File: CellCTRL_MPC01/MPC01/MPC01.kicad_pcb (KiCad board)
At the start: 4 copper layers, 95.8 x 62 mm, 51 parts, among them J1 Power 24V, J10 Microstepping, J11 Microstepping, J12 StepMotor 1, J13 StepMotor 2, J14 StepMotor 3, J15 StepMotor 4, J16 Conn_01x05_Pin, J2 Conn_01x03_Pin, J3 Servo Motor 1u2, J4 Endstop X, J5 Endstop Y, J6 Endstop Z, J7 0Ohm Jumper, J8 Microstepping, J9 Microstepping, U1 TP8485E-SR

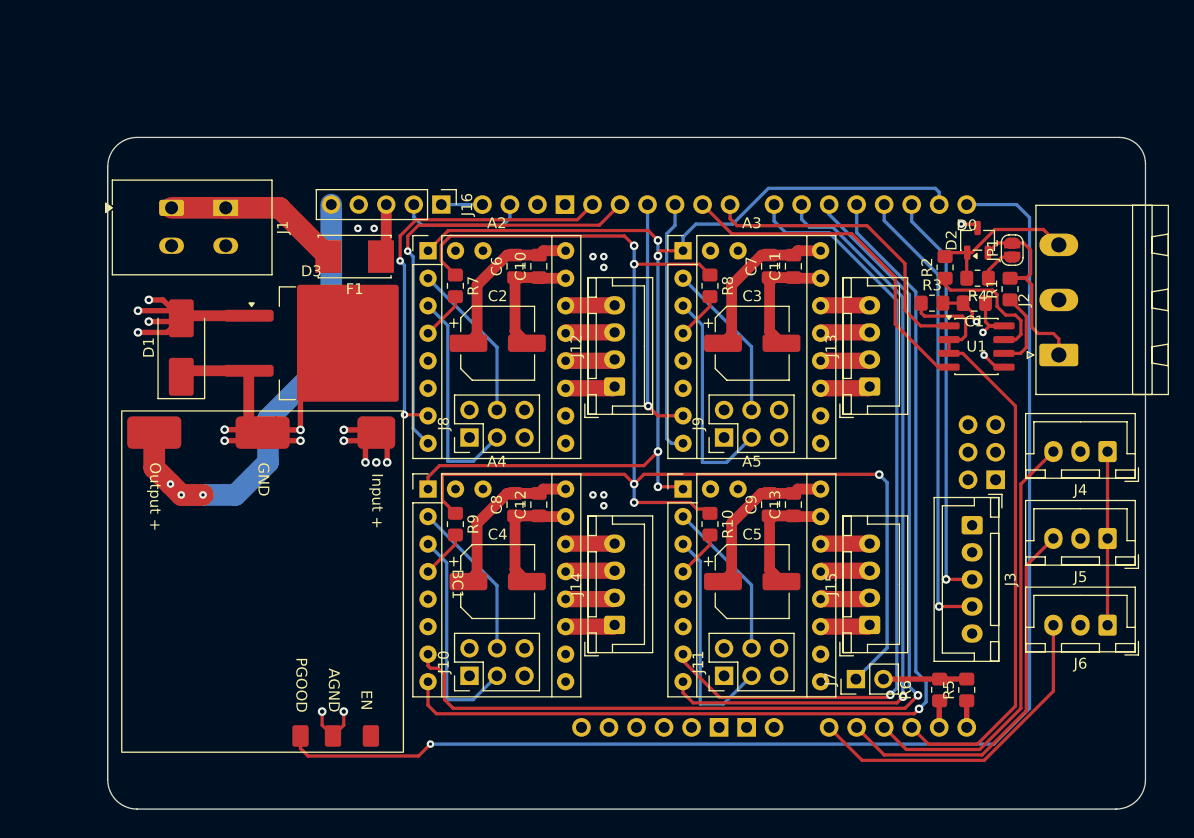
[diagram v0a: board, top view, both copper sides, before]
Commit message: Silkscreen Add Files
Hinzufügen der Beschriftungen auf dem Silkscreen FRont and Back
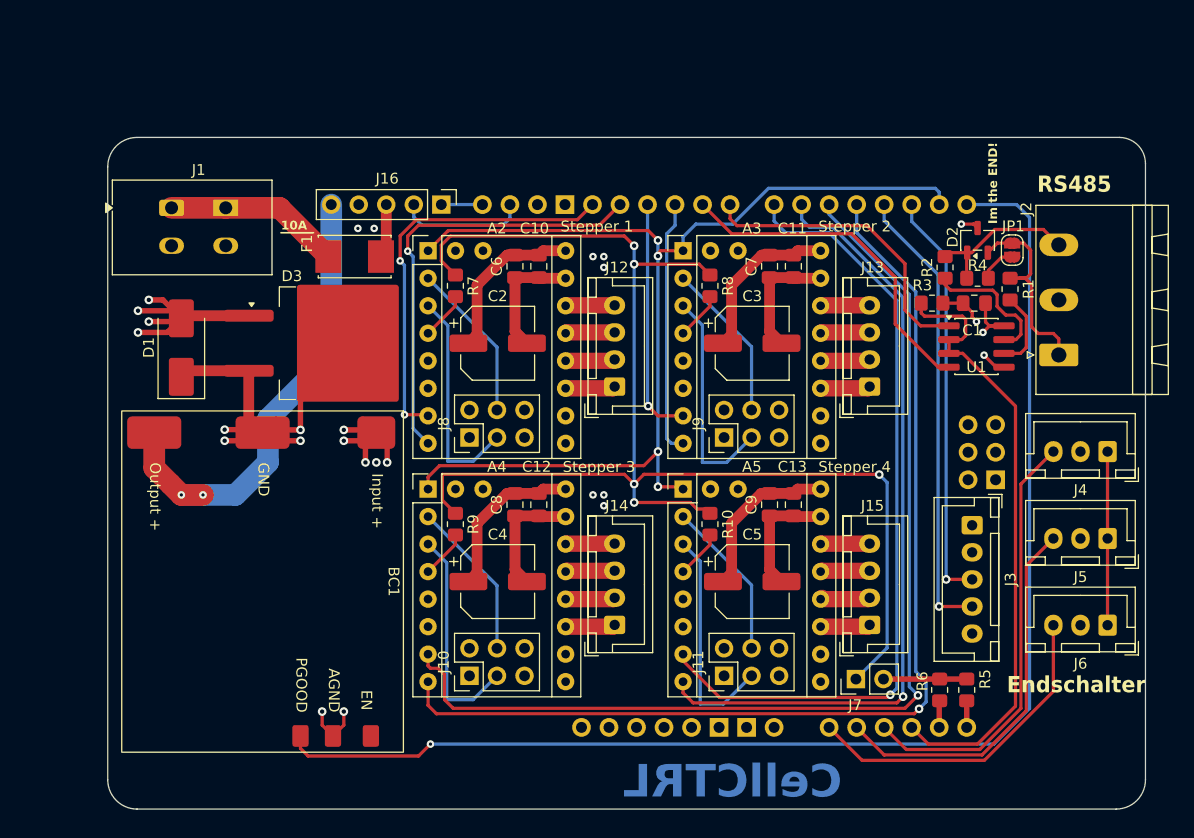
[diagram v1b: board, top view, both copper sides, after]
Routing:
- net 5V: vias 4 -> 3
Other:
- board text added: "10A"
- board text added: "2026/02 V0.1b Edited by: KJ"
- board text added: "CellCTRL"
- board text added: "Endschalter"
- board text added: "Im the END!"
- board text added: "MPC01"
- board text added: "RS485"
- board text added: "Stepper 1"
- board text added: "Stepper 2"
- board text added: "Stepper 3"
- board text added: "Stepper 4"
- board text added: "This Product is designed and made for KTLA/Litec"

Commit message: Update MPC01
MPC01 update
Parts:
- removed A5: TMC2209, MPC01_lib:TMC2209
- removed C11, C12, C13: 4,7uF, Capacitor_SMD:C_0805_2012Metric_Pad1.18x1.45mm_HandSolder
- removed J12: StepMotor 1, Connector_JST:JST_XH_B4B-XH-A_1x04_P2.50mm_Vertical
- removed J13: StepMotor 2, Connector_JST:JST_XH_B4B-XH-A_1x04_P2.50mm_Vertical
- removed J14: StepMotor 3, Connector_JST:JST_XH_B4B-XH-A_1x04_P2.50mm_Vertical
- removed J15: StepMotor 4, Connector_JST:JST_XH_B4B-XH-A_1x04_P2.50mm_Vertical
- removed J16: Conn_01x05_Pin, Connector_PinHeader_2.54mm:PinHeader_1x05_P2.54mm_Vertical
- added JP10: Jumper_2_Open, Jumper:SolderJumper-2_P1.3mm_Open_RoundedPad1.0x1.5mm, F.Cu at (137.1, 50.2)
- added JP2: MS1, Connector_PinHeader_2.54mm:PinHeader_1x02_P2.54mm_Vertical, F.Cu at (95.5, 71.7)
- added JP3: MS1, Connector_PinHeader_2.54mm:PinHeader_1x02_P2.54mm_Vertical, F.Cu at (121.5, 71.7)
- added JP4: MS2, Connector_PinHeader_2.54mm:PinHeader_1x02_P2.54mm_Vertical, F.Cu at (102.5, 45.4)
- added JP5: MS2, Connector_PinHeader_2.54mm:PinHeader_1x02_P2.54mm_Vertical, F.Cu at (95.5, 68.1)
- added JP6: MS2, Connector_PinHeader_2.54mm:PinHeader_1x02_P2.54mm_Vertical, F.Cu at (121.5, 68.1)
- added JP7: Jumper_3_Open, PCM_SparkFun-Jumper:Jumper_3_NO, F.Cu at (96.8, 51.6)
- added JP8: Jumper_3_Open, PCM_SparkFun-Jumper:Jumper_3_NO, F.Cu at (89.8, 74.3)
- added JP9: Jumper_3_Open, PCM_SparkFun-Jumper:Jumper_3_NO, F.Cu at (115.8, 74.3)
- added R11: 120R, Resistor_SMD:R_0805_2012Metric_Pad1.20x1.40mm_HandSolder, F.Cu at (136.6, 46.2)
- added R12: 10R, Resistor_SMD:R_0805_2012Metric_Pad1.20x1.40mm_HandSolder, F.Cu at (134.6, 46.2)
- added R13: 10K, Resistor_SMD:R_0805_2012Metric_Pad1.20x1.40mm_HandSolder, F.Cu at (129.6, 52.2)
- added R14: 10K, Resistor_SMD:R_0805_2012Metric_Pad1.20x1.40mm_HandSolder, F.Cu at (116.0, 59.2)
- added R15: 1K, Resistor_SMD:R_0805_2012Metric_Pad1.20x1.40mm_HandSolder, F.Cu at (118.0, 61.3)
- added R16: 1K, Resistor_SMD:R_0805_2012Metric_Pad1.20x1.40mm_HandSolder, F.Cu at (118.8, 43.5)
- added R17: 1K, Resistor_SMD:R_0805_2012Metric_Pad1.20x1.40mm_HandSolder, F.Cu at (118.8, 41.4)
- A1: value Arduino_Uno_R3_Shield -> TMC2209; footprint PCM_arduino-library:Arduino_Uno_R3_Shield -> MPC01_lib:TMC2209
- A4: value TMC2209 -> Arduino_Uno_R3_Shield; footprint MPC01_lib:TMC2209 -> PCM_arduino-library:Arduino_Uno_R3_Shield
- C1: value 100n -> 100uf; footprint Capacitor_SMD:C_0805_2012Metric_Pad1.18x1.45mm_HandSolder -> Capacitor_SMD:CP_Elec_6.3x7.7
- C10: value 4,7uF -> 100n
- C2, C5: value 100uf -> 1uF; footprint Capacitor_SMD:CP_Elec_6.3x7.7 -> Capacitor_SMD:C_0805_2012Metric_Pad1.18x1.45mm_HandSolder
- C3: value 100uf -> 4,7uF; footprint Capacitor_SMD:CP_Elec_6.3x7.7 -> Capacitor_SMD:C_0805_2012Metric_Pad1.18x1.45mm_HandSolder
- C6, C9: value 1uF -> 4,7uF
- C7: value 1uF -> 100uf; footprint Capacitor_SMD:C_0805_2012Metric_Pad1.18x1.45mm_HandSolder -> Capacitor_SMD:CP_Elec_6.3x7.7
- D1: value D_TVS -> SM712_SOT23; footprint Diode_SMD:D_SMB_Handsoldering -> Package_TO_SOT_SMD:SOT-23-3
- D2: value SM712_SOT23 -> D_TVS; footprint Package_TO_SOT_SMD:SOT-23-3 -> Diode_SMD:D_SMB_Handsoldering
- J1: value Power 24V -> StepMotor 1; footprint TerminalBlock_WAGO:TerminalBlock_WAGO_2601-1102_1x02_P3.50mm_Horizontal -> Connector_JST:JST_XH_B4B-XH-A_1x04_P2.50mm_Vertical
- J10: value Microstepping -> Enable/Disable; footprint MPC01_lib:PinHeader_2x03_P2.54mm_Vertical_ Pinorder -> Connector_JST:JST_XH_B2B-XH-A_1x02_P2.50mm_Vertical
- J11: value Microstepping -> Endstop Z; footprint MPC01_lib:PinHeader_2x03_P2.54mm_Vertical_ Pinorder -> Connector_JST:JST_XH_B3B-XH-A_1x03_P2.50mm_Vertical
- J2: value Conn_01x03_Pin -> StepMotor 2; footprint Connector_Phoenix_MSTB:PhoenixContact_MSTBA_2,5_3-G-5,08_1x03_P5.08mm_Horizontal -> Connector_JST:JST_XH_B4B-XH-A_1x04_P2.50mm_Vertical
- J3: value Servo Motor 1u2 -> StepMotor 3; footprint Connector_JST:JST_XH_B5B-XH-A_1x05_P2.50mm_Vertical -> Connector_JST:JST_XH_B4B-XH-A_1x04_P2.50mm_Vertical
- J4: value Endstop X -> Conn_01x03_Pin; footprint Connector_JST:JST_XH_B3B-XH-A_1x03_P2.50mm_Vertical -> Connector_Phoenix_MSTB:PhoenixContact_MSTBA_2,5_3-G-5,08_1x03_P5.08mm_Horizontal
- J5: value Endstop Y -> I2C; footprint Connector_JST:JST_XH_B3B-XH-A_1x03_P2.50mm_Vertical -> Connector_JST:JST_XH_B5B-XH-A_1x05_P2.50mm_Vertical
- J6: value Endstop Z -> Endstop X
- J7: value 0Ohm Jumper -> Power 24V; footprint Connector_PinHeader_2.54mm:PinHeader_1x02_P2.54mm_Vertical -> TerminalBlock_WAGO:TerminalBlock_WAGO_2601-1102_1x02_P3.50mm_Horizontal
- J8: value Microstepping -> 0Ohm Jumper; footprint MPC01_lib:PinHeader_2x03_P2.54mm_Vertical_ Pinorder -> Connector_PinHeader_2.54mm:PinHeader_1x02_P2.54mm_Vertical
- J9: value Microstepping -> Endstop Y; footprint MPC01_lib:PinHeader_2x03_P2.54mm_Vertical_ Pinorder -> Connector_JST:JST_XH_B3B-XH-A_1x03_P2.50mm_Vertical
- JP1: value Jumper_2_Open -> MS1; footprint Jumper:SolderJumper-2_P1.3mm_Open_RoundedPad1.0x1.5mm -> Connector_PinHeader_2.54mm:PinHeader_1x02_P2.54mm_Vertical
- R1, R2: value 10R -> 10K
- R10: value 1K -> 10R
- R4: value 120R -> 10K
- R5, R6: value 1K -> 10K
- moved J7 81.6 mm to (68.0, 44.0), turned to 180 degrees
- moved D1 69.6 mm to (137.5, 41.9)
- moved D2 69.5 mm to (76.0, 40.5), turned to 0 degrees
- moved A1 61.5 mm to (97.8, 41.1)
- moved R1 58.5 mm to (89.8, 66.8), turned to -90 degrees
- moved R4 56.6 mm to (89.8, 70.8), turned to 90 degrees
- moved J1 47.0 mm to (116.8, 55.1), turned to 90 degrees
- moved R3 45.8 mm to (96.8, 44.1), turned to -90 degrees
- moved JP1 45.5 mm to (102.5, 49.0)
- moved R2 45.3 mm to (96.8, 48.1)
- moved J2 44.5 mm to (110.0, 77.8)
- moved J10 43.6 mm to (124.0, 58.0), turned to 0 degrees
- moved J11 38.9 mm to (143.0, 60.5), turned to 0 degrees
- moved C1 37.5 mm to (106.8, 56.6), turned to -90 degrees
- moved R6 37.1 mm to (115.8, 66.8), turned to -90 degrees
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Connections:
- A2 pad 5: unconnected-(A2-TX-Pad5) -> Net-(A2-TX)
- A2 pad 7: STEP1 -> STEP2
- A2 pad 8: DIR1 -> DIR2
- A3 pad 5: unconnected-(A3-TX-Pad5) -> Net-(A3-TX)
- A3 pad 7: STEP2 -> STEP3
- A3 pad 8: DIR2 -> DIR3
- C1 pad 1: 5V -> +24V
- C10 pad 1: GND -> 5V
- C10 pad 2: +24V -> GND
- C2 pad 1: +24V -> GND
- C2 pad 2: GND -> +24V
- C3 pad 1: +24V -> GND
- C3 pad 2: GND -> +24V
- C5 pad 1: +24V -> GND
- C5 pad 2: GND -> +24V
- C7 pad 1: GND -> +24V
- C7 pad 2: +24V -> GND
- D1 pad 1: GND -> Net-(D1-A1)
- D1 pad 2: +24V -> Net-(D1-A2)
- D2 pad 1: Net-(D2-A1) -> GND
- D2 pad 2: Net-(D2-A2) -> +24V
- F1 pad 2: Net-(J1-Pin_1) -> Net-(J7-Pin_1)
- J1 pad 1: Net-(J1-Pin_1) -> Net-(A1-B2)
- J1 pad 2: GND -> Net-(A1-B1)
- J10 pad 1: 5V -> ENABLE
- J10 pad 2: Net-(A4-MS2) -> GND
- J11 pad 1: 5V -> Net-(J11-Pin_1)
- J11 pad 2: Net-(A5-MS2) -> GND
- J11 pad 3: GND -> EndstopZ
- J2 pad 1: Net-(D2-A2) -> Net-(A2-B2)
- J2 pad 2: GND -> Net-(A2-B1)
- J2 pad 3: Net-(D2-A1) -> Net-(A2-A1)
- J3 pad 1: GND -> Net-(A3-B2)
- J3 pad 2: 5V -> Net-(A3-B1)
- J3 pad 3: Motor1 -> Net-(A3-A1)
- J3 pad 4: Motor2 -> Net-(A3-A2)
- J4 pad 1: Net-(J4-Pin_1) -> Net-(D1-A2)
- J4 pad 3: EndstopX -> Net-(D1-A1)
- J5 pad 1: Net-(J4-Pin_1) -> Net-(J5-Pin_1)
- J5 pad 2: GND -> Net-(J5-Pin_2)
- J5 pad 3: EndstopY -> +24V
- J6 pad 1: Net-(J4-Pin_1) -> Net-(J11-Pin_1)
- J6 pad 3: EndstopZ -> EndstopX
- J7 pad 1: PDNUart -> Net-(J7-Pin_1)
- J7 pad 2: Net-(J7-Pin_2) -> GND
- J8 pad 1: 5V -> PDNUart
- J8 pad 2: Net-(A2-MS2) -> Net-(J8-Pin_2)
- J9 pad 1: 5V -> Net-(J11-Pin_1)
- J9 pad 2: Net-(A3-MS2) -> GND
- J9 pad 3: GND -> EndstopY
- JP1 pad 1: Net-(JP1-A) -> Net-(A1-MS2)
- JP1 pad 2: Net-(D2-A2) -> 5V
- R1 pad 1: RS485_A -> GND
- R1 pad 2: Net-(D2-A2) -> Net-(A2-MS1)
- R10 pad 1: PDNUart -> RS485_A
- R10 pad 2: Net-(A5-RX) -> Net-(D1-A2)
- R2 pad 1: RS485_B -> GND
- R2 pad 2: Net-(D2-A1) -> Net-(A1-MS2)
- R3 pad 1: RS485_DE/RE -> GND
- R3 pad 2: GND -> Net-(A1-MS1)
- R4 pad 1: Net-(JP1-A) -> GND
- R4 pad 2: Net-(D2-A1) -> Net-(A2-MS2)
- R5 pad 1: RX -> GND
- R5 pad 2: Net-(J7-Pin_2) -> Net-(A3-MS2)
- R6 pad 1: TX -> GND
- R6 pad 2: Net-(J7-Pin_2) -> Net-(A3-MS1)
- R7 pad 1: PDNUart -> Net-(JP7-C)
- R7 pad 2: Net-(A2-RX) -> PDNUart
- R8 pad 1: PDNUart -> Net-(JP8-C)
- R8 pad 2: Net-(A3-RX) -> PDNUart
- R9 pad 1: PDNUart -> Net-(JP9-C)
- R9 pad 2: Net-(A4-RX) -> PDNUart
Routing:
- net STEP4: track 73.8 -> 0.00 mm, vias 1 -> 0
- net DIR4: track 72.5 -> 0.00 mm, vias 1 -> 0
- net PGOOD: track 122.2 -> 66.9 mm, vias 1 -> 2
- net STEP2: track 22.2 -> 72.4 mm, vias 1 -> 3
- net DIR2: track 23.6 -> 73.5 mm, vias 0 -> 3
- net Motor2: track 42.3 -> 0.00 mm, vias 1 -> 0
- net STEP3: track 98.5 -> 56.9 mm
- net DIR3: track 97.5 -> 56.4 mm
- net ENABLEOut: track 0.00 -> 39.3 mm, vias 0 -> 3
- net GND: track 99.2 -> 137.6 mm, vias 9 -> 12
- net Motor1: track 38.3 -> 0.00 mm, vias 1 -> 0
- net ENABLE: track 101.6 -> 66.4 mm, vias 4 -> 2
- net 5V: track 50.0 -> 15.8 mm
- net Net-(A5-MS2): track 21.2 -> 0.00 mm
- net Net-(A4-MS2): track 20.6 -> 0.00 mm
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- removed copper zone on In2.Cu, net +24V
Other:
- board size 95.8 x 62 mm -> 90.3 x 53.4 mm
- board text added: "(I2C)"
- board text added: "24V"
- board text added: "5V"
- board text added: "GND"
- board text added: "Motor 1 (X)"
- board text added: "Motor 2 (Y)"
- board text added: "Motor 3 (Z)"
- board text added: "Power In (24V DC)"
- board text added: "SCL"
- board text added: "SDA"
- board text added: "X-Endstop"
- board text added: "Y-Endstop"
- board text added: "Z-Endstop"
- board text removed: "10A"
- board text removed: "2026/02 V0.1b Edited by: KJ"
- board text removed: "CellCTRL"
- board text removed: "Endschalter"
- board text removed: "Im the END!"
- board text removed: "MPC01"
- board text removed: "Stepper 1"
- board text removed: "Stepper 2"
- board text removed: "Stepper 3"
- board text removed: "Stepper 4"
- board text removed: "This Product is designed and made for KTLA/Litec"

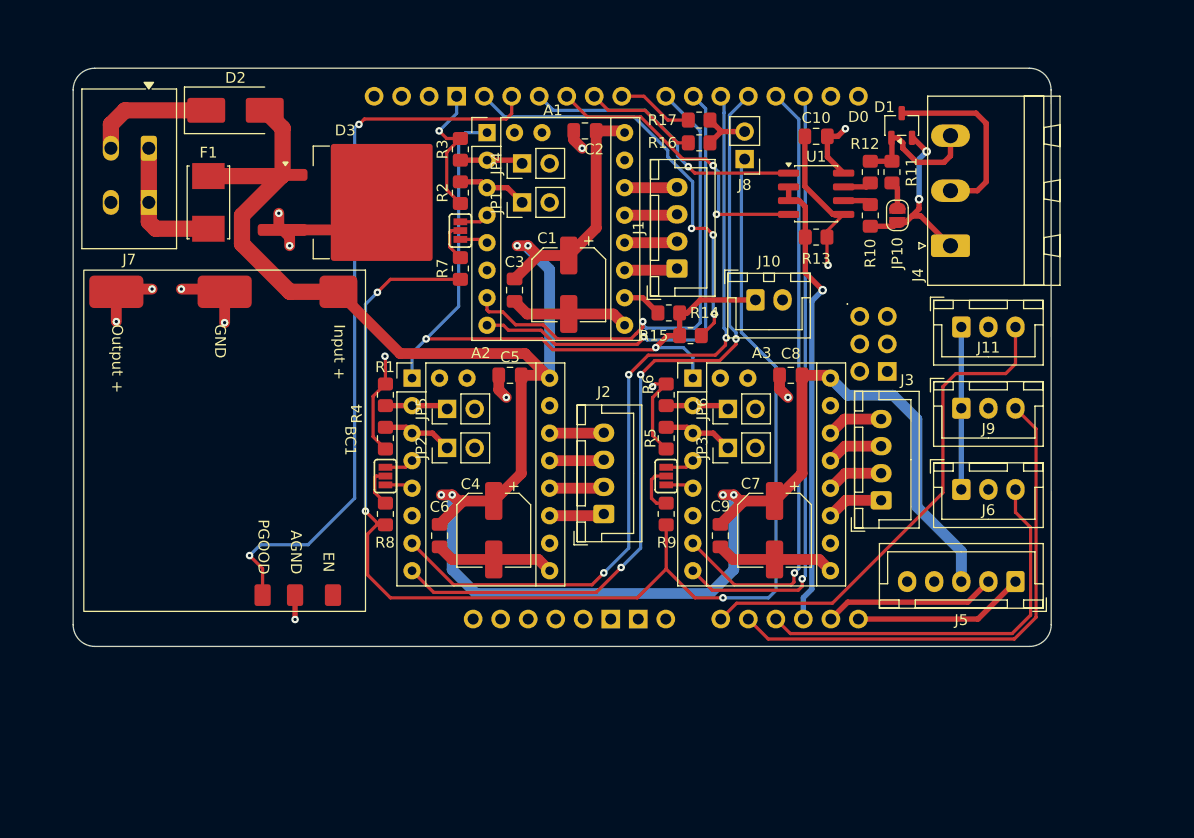
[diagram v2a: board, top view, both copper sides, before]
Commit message: Mounting Hole adds
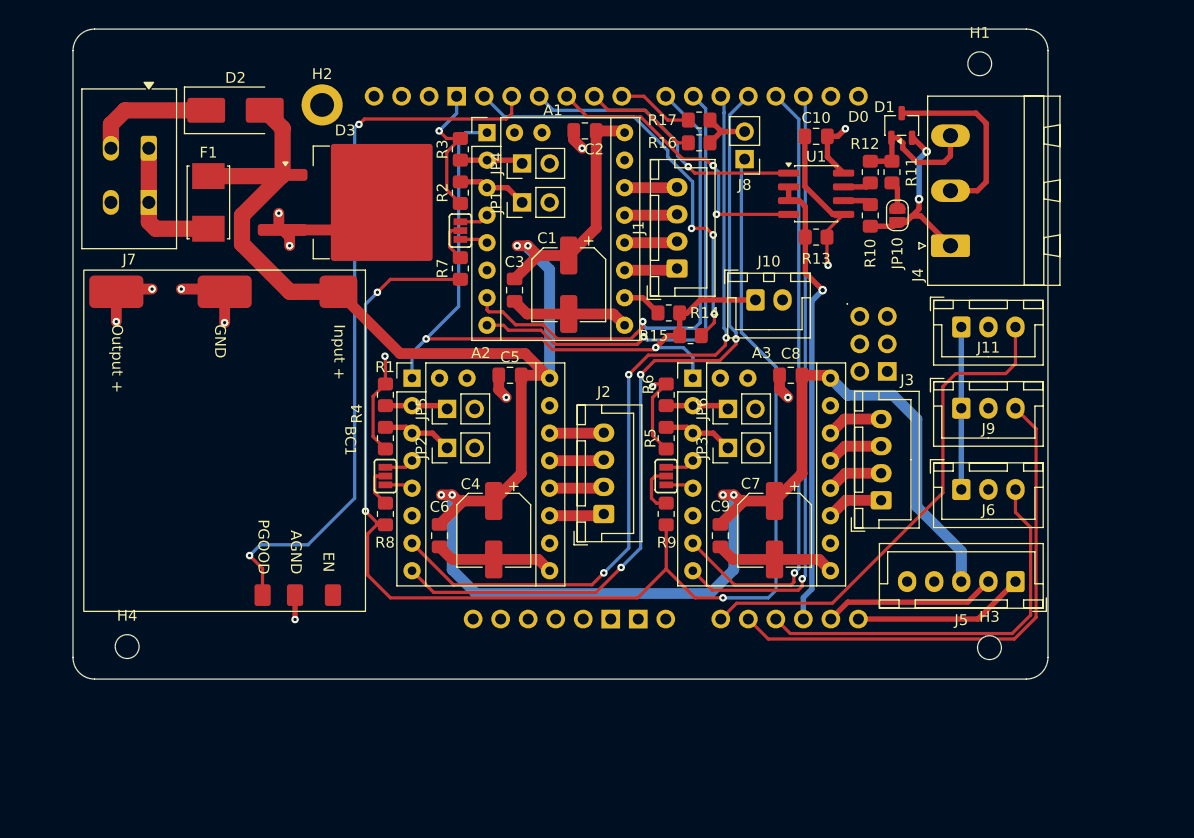
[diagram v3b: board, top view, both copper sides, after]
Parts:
- added H1: MountingHole, MountingHole:MountingHole_2.2mm_M2_DIN965, F.Cu at (144.7, 36.2)
- added H2: MountingHole_Pad, MountingHole:MountingHole_2.2mm_M2_DIN965_Pad, F.Cu at (84.0, 40.0)
- added H3: MountingHole, MountingHole:MountingHole_2.2mm_M2_DIN965, F.Cu at (145.6, 90.1)
- added H4: MountingHole, MountingHole:MountingHole_2.2mm_M2_DIN965, F.Cu at (66.0, 90.0)
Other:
- board size 90.3 x 53.4 mm -> 90 x 60 mm

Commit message: Maße
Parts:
- moved H2 18.6 mm to (66.0, 35.5)
- moved H1 1.48 mm to (146.0, 35.5)
- moved H3 0.72 mm to (146.0, 89.5)
- moved H4 0.50 mm to (66.0, 89.5)
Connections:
- A4 pad A4: Net-(J5-Pin_2) -> Net-(J5-Pin_1)
- A4 pad A5: Net-(J5-Pin_1) -> Net-(J5-Pin_2)
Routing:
- net Net-(J5-Pin_1): track 15.9 -> 20.2 mm
- net Net-(J5-Pin_2): track 16.0 -> 13.4 mm
- net EndstopX: track 37.0 -> 36.3 mm
- net EndstopY: track 48.2 -> 47.7 mm
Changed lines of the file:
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@@
 			(layers "*.Cu" "*.Mask")
 			(remove_unused_layers no)
-			(net 66 "Net-(J5-Pin_2)")
+			(net 58 "Net-(J5-Pin_1)")
 			(pinfunction "A4")
 			(pintype "bidirectional")
@@
 			(layers "*.Cu" "*.Mask")
 			(remove_unused_layers no)
-			(net 58 "Net-(J5-Pin_1)")
+			(net 66 "Net-(J5-Pin_2)")
 			(pinfunction "A5")
 			(pintype "bidirectional")
@@
 	(footprint "MountingHole:MountingHole_2.2mm_M2_DIN965_Pad"
 		(layer "F.Cu")
-		(at 84 40)
+		(at 66 35.5)
 		(descr "Mounting Hole 2.2mm, M2, generated by kicad-footprint-generator mountinghole.py")
 		(tags "mountinghole M2 DIN965")
 		(property "Reference" "H2"
-			(at 0 -2.85 0)
+			(at -3.5 0 0)
 			(layer "F.SilkS")
 			(effects
@@
 	(footprint "MountingHole:MountingHole_2.2mm_M2_DIN965"
 		(layer "F.Cu")
-		(at 145.6 90.1)
+		(at 146 89.5)
 		(descr "Mounting Hole 2.2mm, M2, no annular, generated by kicad-footprint-generator mountinghole.py")
 		(tags "mountinghole M2 DIN965")
 		(property "Reference" "H3"
-			(at 0 -2.85 0)
+			(at -4 0 0)
 			(layer "F.SilkS")
 			(effects
@@
 	(footprint "MountingHole:MountingHole_2.2mm_M2_DIN965"
 		(layer "F.Cu")
-		(at 66 90)
+		(at 66 89.5)
 		(descr "Mounting Hole 2.2mm, M2, no annular, generated by kicad-footprint-generator mountinghole.py")
 		(tags "mountinghole M2 DIN965")
 		(property "Reference" "H4"
-			(at 0 -2.85 0)
+			(at -3.5 0 0)
 			(layer "F.SilkS")
 			(effects
@@
 	(footprint "MountingHole:MountingHole_2.2mm_M2_DIN965"
 		(layer "F.Cu")
-		(at 144.7 36.2)
+		(at 146 35.5)
 		(descr "Mounting Hole 2.2mm, M2, no annular, generated by kicad-footprint-generator mountinghole.py")
 		(tags "mountinghole M2 DIN965")
 		(property "Reference" "H1"
-			(at 0 -2.85 0)
+			(at -4 0 0)
 			(layer "F.SilkS")
 			(effects
@@
 	)
 	(segment
-		(start 149.9 87.3)
-		(end 149.9 69.9)
+		(start 125.38 89.5)
+		(end 127.21148 89.5)
+		(width 0.3)
+		(layer "F.Cu")
+		(net 1)
+	)
+	(segment
+		(start 127.21148 89.5)
+		(end 127.41248 89.701)
 		(width 0.3)
 		(layer "F.Cu")
@@
 	)
 	(segment
-		(start 147.9 89.3)
-		(end 149.9 87.3)
+		(start 145.408521 86.8)
+		(end 148.9 86.8)
+		(width 0.3)
+		(layer "F.Cu")
+		(net 1)
+	)
+	(segment
+		(start 149.9 69.9)
+		(end 148 68)
 		(width 0.3)
 		(layer "F.Cu")
@@
 	(segment
 		(start 123.34 87.46)
-		(end 125.18 89.3)
+		(end 125.38 89.5)
 		(width 0.3)
 		(layer "F.Cu")
@@
 	)
 	(segment
-		(start 125.18 89.3)
-		(end 147.9 89.3)
+		(start 142.507521 89.701)
+		(end 145.408521 86.8)
 		(width 0.3)
 		(layer "F.Cu")
@@
 	)
 	(segment
-		(start 149.9 69.9)
-		(end 148 68)
+		(start 149.9 85.8)
+		(end 149.9 69.9)
+		(width 0.3)
+		(layer "F.Cu")
+		(net 1)
+	)
+	(segment
+		(start 127.41248 89.701)
+		(end 142.507521 89.701)
+		(width 0.3)
+		(layer "F.Cu")
+		(net 1)
+	)
+	(segment
+		(start 148.9 86.8)
+		(end 149.9 85.8)
 		(width 0.3)
 		(layer "F.Cu")
@@
 	)
 	(segment
-		(start 147.69248 88.799)
-		(end 149.399 87.09248)
+		(start 148 77.601)
+		(end 149.399 79)
 		(width 0.3)
 		(layer "F.Cu")
@@
 	)
 	(segment
-		(start 148 77.601)
-		(end 148 75.5)
+		(start 149.399 85.401)
+		(end 148.5 86.3)
 		(width 0.3)
 		(layer "F.Cu")
@@
 	)
 	(segment
-		(start 127.219 88.799)
-		(end 147.69248 88.799)
+		(start 142.3 89.2)
+		(end 127.62 89.2)
 		(width 0.3)
 		(layer "F.Cu")
@@
 	)
 	(segment
-		(start 125.88 87.46)
-		(end 127.219 88.799)
+		(start 149.399 79)
+		(end 149.399 85.401)
 		(width 0.3)
 		(layer "F.Cu")
@@
 	)
 	(segment
-		(start 149.399 87.09248)
-		(end 149.399 79)
+		(start 145.2 86.3)
+		(end 142.3 89.2)
 		(width 0.3)
 		(layer "F.Cu")
@@
 	)
 	(segment
-		(start 149.399 79)
+		(start 148 75.5)
 		(end 148 77.601)
 		(width 0.3)
@@
 	)
 	(segment
+		(start 148.5 86.3)
+		(end 145.2 86.3)
+		(width 0.3)
+		(layer "F.Cu")
+		(net 24)
+	)
+	(segment
+		(start 127.62 89.2)
+		(end 125.88 87.46)
+		(width 0.3)
+		(layer "F.Cu")
+		(net 24)
+	)
+	(segment
 		(start 89.84 75.0728)
 		(end 91.9928 75.0728)
@@
 	)
 	(segment
-		(start 148 84)
-		(end 144.54 87.46)
-		(width 0.5)
+		(start 130.96 87.46)
+		(end 132.1746 88.6746)
+		(width 0.3)
 		(layer "F.Cu")
 		(net 58)
 	)
 	(segment
-		(start 144.54 87.46)
-		(end 133.5 87.46)
-		(width 0.5)
+		(start 132.1746 88.6746)
+		(end 142.0254 88.6746)
+		(width 0.3)
 		(layer "F.Cu")
 		(net 58)
 	)
 	(segment
-		(start 143.6 85.9)
-		(end 145.5 84)
-		(width 0.5)
+		(start 144.9 85.8)
+		(end 147.4 85.8)
+		(width 0.3)
 		(layer "F.Cu")
-		(net 66)
+		(net 58)
 	)
 	(segment
-		(start 132.52 85.9)
-		(end 143.6 85.9)
-		(width 0.5)
+		(start 148 85.2)
+		(end 148 84)
+		(width 0.3)
+		(layer "F.Cu")
+		(net 58)
+	)
+	(segment
+		(start 142.0254 88.6746)
+		(end 144.9 85.8)
+		(width 0.3)
+		(layer "F.Cu")
+		(net 58)
+	)
+	(segment
+		(start 147.4 85.8)
+		(end 148 85.2)
+		(width 0.3)
+		(layer "F.Cu")
+		(net 58)
+	)
+	(segment
+		(start 133.5 87.46)
+		(end 142.04 87.46)
+		(width 0.3)
 		(layer "F.Cu")
 		(net 66)
 	)
 	(segment
-		(start 130.96 87.46)
-		(end 132.52 85.9)
-		(width 0.5)
+		(start 142.04 87.46)
+		(end 145.5 84)
+		(width 0.3)
 		(layer "F.Cu")
 		(net 66)

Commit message: Fertig V0.1_MPC01
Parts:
- H1, H3, H4: value MountingHole -> MountingHole_Pad; footprint MountingHole:MountingHole_2.2mm_M2_DIN965 -> MountingHole:MountingHole_2.2mm_M2_DIN965_Pad
- moved J7 7.22 mm to (67.6, 51.2), turned to 90 degrees
- moved F1 2.10 mm to (75.6, 49.0)
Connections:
- H2 pad 1: unconnected-(H2-Pad1) -> GND
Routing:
- net GND: track 137.6 -> 147.8 mm
- net Net-(JP7-C): track 3.81 -> 5.41 mm
- net Net-(JP8-C): track 3.81 -> 4.99 mm
- net +24V: track 206.3 -> 206.9 mm, vias 6 -> 8
- net Net-(J7-Pin_1): track 12.6 -> 13.1 mm
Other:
- board text added: "Control Board (CellCTRL) V0.1 03/2026 Edit by JK github.com/Kappi084/CellCTRL"
- board text added: "ENABLE"
- board text added: "MPC01"
- board text added: "PDNUart"
- board text added: "RS484 B"
- board text added: "RS485 A"
- board text added: "TMC2209"
